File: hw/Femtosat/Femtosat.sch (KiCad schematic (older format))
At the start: 9 parts, among them J2 Programmer, U1 SAMD21G, U2 TRH-G2, U3 XA1110, Y1 32.768kHz

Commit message: Added library for certain components. Symbols and footprints were associated.
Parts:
- Cc1, Cc2: footprint Capacitor_SMD:C_0805_2012Metric_Pad1.15x1.40mm_HandSolder -> Capacitor_SMD:C_0603_1608Metric_Pad1.05x0.95mm_HandSolder
- J2: footprint (none) -> Connector_PinSocket_2.54mm:PinSocket_1x03_P2.54mm_Vertical
- U2: footprint (none) -> GPS:TRH-G2
- U3: footprint (none) -> GPS:XA1110
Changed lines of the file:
@@
 F 0 "Cc1" H 3215 2446 50  0000 L CNN
 F 1 "9pF" H 3215 2355 50  0000 L CNN
-F 2 "Capacitor_SMD:C_0805_2012Metric_Pad1.15x1.40mm_HandSolder" H 3138 2250 50  0001 C CNN
+F 2 "Capacitor_SMD:C_0603_1608Metric_Pad1.05x0.95mm_HandSolder" H 3138 2250 50  0001 C CNN
 F 3 "~" H 3100 2400 50  0001 C CNN
 	1    3100 2400
@@
 F 0 "Cc2" H 3715 2446 50  0000 L CNN
 F 1 "9pF" H 3715 2355 50  0000 L CNN
-F 2 "Capacitor_SMD:C_0805_2012Metric_Pad1.15x1.40mm_HandSolder" H 3638 2250 50  0001 C CNN
+F 2 "Capacitor_SMD:C_0603_1608Metric_Pad1.05x0.95mm_HandSolder" H 3638 2250 50  0001 C CNN
 F 3 "~" H 3600 2400 50  0001 C CNN
 	1    3600 2400
@@
 F 0 "U3" H 7600 5050 60  0000 C CNN
 F 1 "XA1110" H 7600 4350 60  0000 C CNN
-F 2 "" H 7300 4650 60  0001 C CNN
+F 2 "GPS:XA1110" H 7300 4650 60  0001 C CNN
 F 3 "" H 7300 4650 60  0001 C CNN
 	1    7600 4700
@@
 F 0 "J2" H 7572 2124 50  0000 R CNN
 F 1 "Programmer" H 7572 2033 50  0000 R CNN
-F 2 "" H 7600 2100 50  0001 C CNN
+F 2 "Connector_PinSocket_2.54mm:PinSocket_1x03_P2.54mm_Vertical" H 7600 2100 50  0001 C CNN
 F 3 "~" H 7600 2100 50  0001 C CNN
 	1    7600 2100
@@
 F 0 "U2" H 7550 3700 50  0000 C CNN
 F 1 "TRH-G2" H 7800 3050 50  0000 C CNN
-F 2 "" H 7650 3350 50  0001 C CNN
+F 2 "GPS:TRH-G2" H 7650 3350 50  0001 C CNN
 F 3 "" H 7650 3350 50  0001 C CNN
 	1    7550 3350

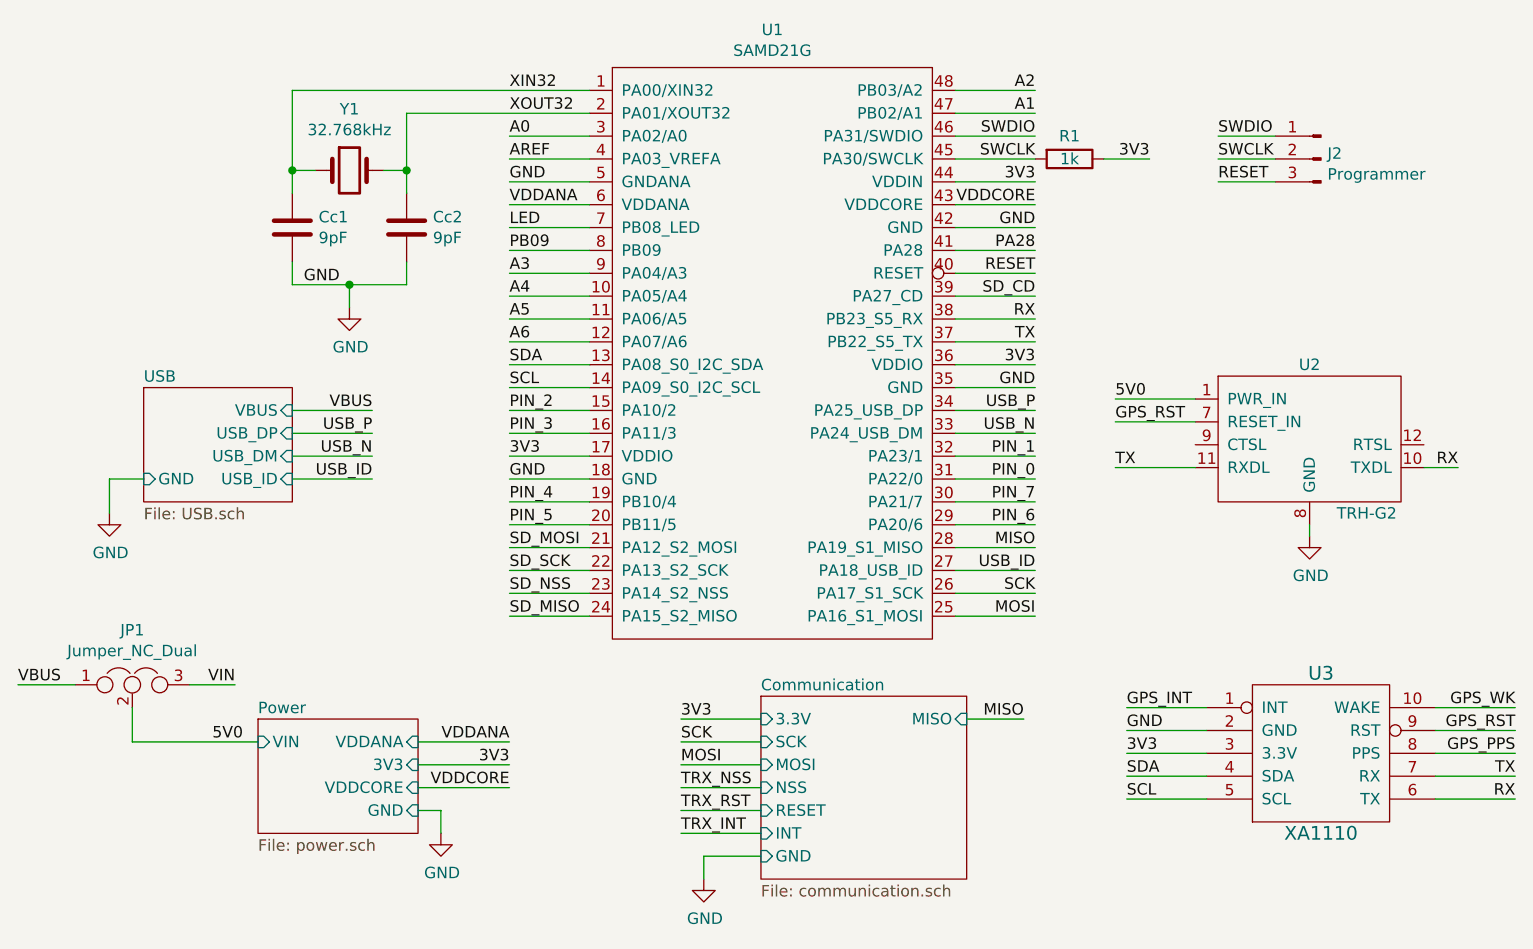
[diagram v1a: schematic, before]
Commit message: Deleted the GPS device (moved to another PCB). Added the deploy-sensor (an interrupter). Moved the programmer to its own hierarchical sheet.
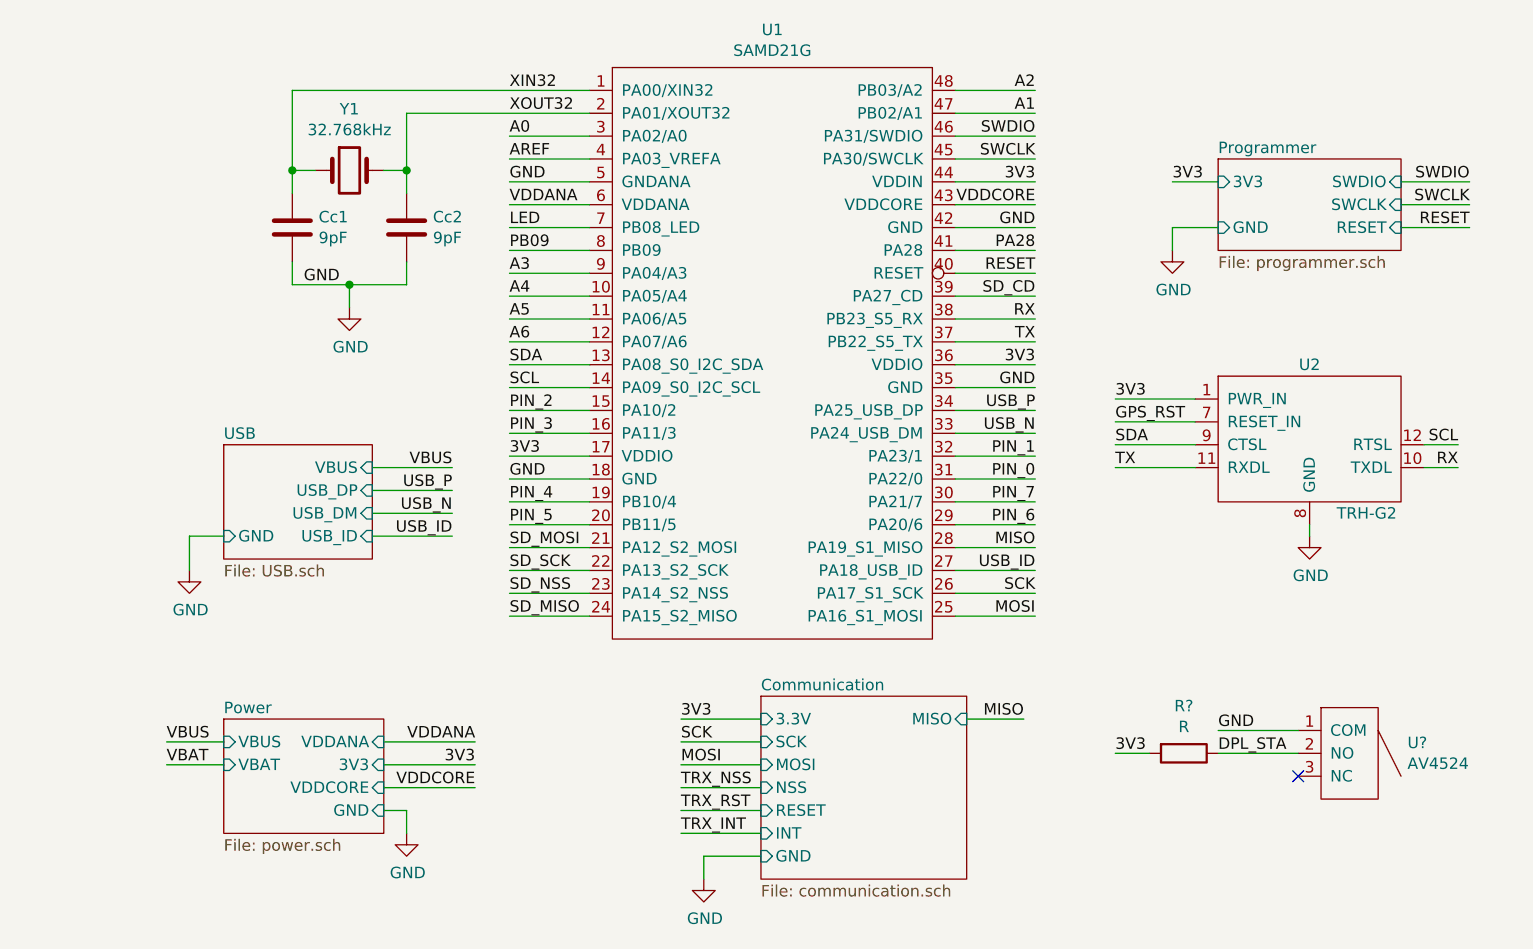
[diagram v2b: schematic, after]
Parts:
- removed J2: Programmer, Connector_PinSocket_2.54mm:PinSocket_1x03_P2.54mm_Vertical, symbol Connector:Conn_01x03_Male
- removed JP1: Jumper_NC_Dual, Connector_PinHeader_2.54mm:PinHeader_1x03_P2.54mm_Vertical, symbol Device:Jumper_NC_Dual
- removed R1: 1k, Resistor_SMD:R_0805_2012Metric_Pad1.15x1.40mm_HandSolder, symbol Device:R
- removed U3: XA1110, GPS:XA1110, symbol GPS:XA1110
- added R?: R, symbol Device:R
- added U?: AV4524, symbol Interrupter:AV4524
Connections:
- net 5V0 is gone; now on net 3V3: U2.1 (PWR_IN), U2.2 (PWR_IN)
- net 3V3: now also R?.2
- net GND: now also U?.1 (COM)
- net SCL: now also U2.12 (RTSL)
- net SDA: now also U2.9 (CTSL)
- new net DPL_STA: R?.1, U?.2 (NO)
- no-connect marks 0 -> 1
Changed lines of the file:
@@
 $Descr A4 11693 8268
 encoding utf-8
-Sheet 1 4
+Sheet 1 5
 Title ""
 Date ""
@@
 	4050 3700 4400 3700
 $Sheet
-S 2950 4550 700  500
+S 2800 4550 700  500
 U 5B6351C6
 F0 "Power" 50
 F1 "power.sch" 50
-F2 "3V3" I R 3650 4750 50
-F3 "VDDANA" I R 3650 4650 50
-F4 "VDDCORE" I R 3650 4850 50
-F5 "GND" I R 3650 4950 50
-F6 "VIN" I L 2950 4650 50
+F2 "3V3" I R 3500 4750 50
+F3 "VDDANA" I R 3500 4650 50
+F4 "VDDCORE" I R 3500 4850 50
+F5 "GND" I R 3500 4950 50
+F6 "VBUS" I L 2800 4650 50
+F7 "VBAT" I L 2800 4750 50
 $EndSheet
-Text Label 4050 4850 2    50   ~ 0
+Text Label 3900 4850 2    50   ~ 0
 VDDCORE
-Text Label 4050 4650 2    50   ~ 0
+Text Label 3900 4650 2    50   ~ 0
 VDDANA
 Wire Wire Line
-	4050 4650 3650 4650
-Wire Wire Line
-	3650 4750 4050 4750
-Wire Wire Line
-	4050 4850 3650 4850
+	3900 4650 3500 4650
+Wire Wire Line
+	3500 4750 3900 4750
+Wire Wire Line
+	3900 4850 3500 4850
 $Comp
 L Device:C Cc1
@@
 Text Label 3150 2650 0    50   ~ 0
 GND
-$Comp
-L Device:R R1
-U 1 1 5B67C5CF
-P 6500 2100
-F 0 "R1" V 6400 2100 50  0000 C CNN
-F 1 "1k" V 6500 2100 50  0000 C CNN
-F 2 "Resistor_SMD:R_0805_2012Metric_Pad1.15x1.40mm_HandSolder" V 6430 2100 50  0001 C CNN
-F 3 "~" H 6500 2100 50  0001 C CNN
-	1    6500 2100
-	0    1    1    0
-$EndComp
-Wire Wire Line
-	6650 2100 6850 2100
-Text Label 6850 2100 2    50   ~ 0
+Text Label 6950 2200 0    50   ~ 0
 3V3
 $Sheet
-S 2450 3100 650  500
+S 2800 3350 650  500
 U 5B626331
 F0 "USB" 50
 F1 "USB.sch" 50
-F2 "VBUS" I R 3100 3200 50
-F3 "USB_DP" I R 3100 3300 50
-F4 "USB_DM" I R 3100 3400 50
-F5 "USB_ID" I R 3100 3500 50
-F6 "GND" I L 2450 3500 50
+F2 "VBUS" I R 3450 3450 50
+F3 "USB_DP" I R 3450 3550 50
+F4 "USB_DM" I R 3450 3650 50
+F5 "USB_ID" I R 3450 3750 50
+F6 "GND" I L 2800 3750 50
 $EndSheet
-Text Label 3450 3300 2    50   ~ 0
+Text Label 3800 3550 2    50   ~ 0
 USB_P
 Wire Wire Line
-	3450 3300 3100 3300
-Wire Wire Line
-	3100 3200 3450 3200
-Wire Wire Line
-	3450 3400 3100 3400
-Wire Wire Line
-	3100 3500 3450 3500
-Text Label 3450 3400 2    50   ~ 0
+	3800 3550 3450 3550
+Wire Wire Line
+	3450 3450 3800 3450
+Wire Wire Line
+	3800 3650 3450 3650
+Wire Wire Line
+	3450 3750 3800 3750
+Text Label 3800 3650 2    50   ~ 0
 USB_N
-Text Label 3450 3500 2    50   ~ 0
+Text Label 3800 3750 2    50   ~ 0
 USB_ID
-Text Label 3450 3200 2    50   ~ 0
+Text Label 3800 3450 2    50   ~ 0
 VBUS
 Wire Wire Line
-	2450 3500 2300 3500
-Wire Wire Line
-	2300 3500 2300 3650
+	2800 3750 2650 3750
+Wire Wire Line
+	2650 3750 2650 3900
 $Comp
 L power:GND #PWR0104
 U 1 1 5BAA2798
-P 2300 3650
-F 0 "#PWR0104" H 2300 3400 50  0001 C CNN
-F 1 "GND" H 2305 3477 50  0000 C CNN
-F 2 "" H 2300 3650 50  0001 C CNN
-F 3 "" H 2300 3650 50  0001 C CNN
-	1    2300 3650
-	1    0    0    -1
-$EndComp
-$Comp
-L Device:Jumper_NC_Dual JP1
-U 1 1 5BADF05F
-P 2400 4400
-F 0 "JP1" H 2400 4639 50  0000 C CNN
-F 1 "Jumper_NC_Dual" H 2400 4548 50  0000 C CNN
-F 2 "Connector_PinHeader_2.54mm:PinHeader_1x03_P2.54mm_Vertical" H 2400 4400 50  0001 C CNN
-F 3 "~" H 2400 4400 50  0001 C CNN
-	1    2400 4400
-	1    0    0    -1
-$EndComp
-Wire Wire Line
-	2150 4400 1900 4400
-Text Label 1900 4400 0    50   ~ 0
+P 2650 3900
+F 0 "#PWR0104" H 2650 3650 50  0001 C CNN
+F 1 "GND" H 2655 3727 50  0000 C CNN
+F 2 "" H 2650 3900 50  0001 C CNN
+F 3 "" H 2650 3900 50  0001 C CNN
+	1    2650 3900
+	1    0    0    -1
+$EndComp
+Text Label 2550 4650 0    50   ~ 0
 VBUS
-Text Label 2850 4400 2    50   ~ 0
-VIN
-Wire Wire Line
-	2850 4400 2650 4400
-Text Label 4050 4750 2    50   ~ 0
-3V3
-Text Label 2750 4650 0    50   ~ 0
-5V0
-Wire Wire Line
-	3650 4950 3750 4950
-Wire Wire Line
-	3750 4950 3750 5050
+Text Label 3900 4750 2    50   ~ 0
+3V3
+Text Label 2550 4750 0    50   ~ 0
+VBAT
+Wire Wire Line
+	3500 4950 3600 4950
+Wire Wire Line
+	3600 4950 3600 5050
 $Comp
 L power:GND #PWR0106
 U 1 1 5BB0EE30
-P 3750 5050
-F 0 "#PWR0106" H 3750 4800 50  0001 C CNN
-F 1 "GND" H 3755 4877 50  0000 C CNN
-F 2 "" H 3750 5050 50  0001 C CNN
-F 3 "" H 3750 5050 50  0001 C CNN
-	1    3750 5050
-	1    0    0    -1
-$EndComp
-Wire Wire Line
-	2400 4650 2950 4650
-Wire Wire Line
-	2400 4500 2400 4650
-Text Label 7150 2000 0    50   ~ 0
+P 3600 5050
+F 0 "#PWR0106" H 3600 4800 50  0001 C CNN
+F 1 "GND" H 3605 4877 50  0000 C CNN
+F 2 "" H 3600 5050 50  0001 C CNN
+F 3 "" H 3600 5050 50  0001 C CNN
+	1    3600 5050
+	1    0    0    -1
+$EndComp
+Text Label 8250 2200 2    50   ~ 0
 SWDIO
-Text Label 7150 2100 0    50   ~ 0
+Text Label 8250 2300 2    50   ~ 0
 SWCLK
-Wire Wire Line
-	7400 2000 7150 2000
-Wire Wire Line
-	7150 2100 7400 2100
 $Sheet
 S 5150 4450 900  800
@@
 Wire Wire Line
 	4900 5150 4900 5250
-$Comp
-L GPS:XA1110 U3
-U 1 1 5BD2F968
-P 7600 4700
-F 0 "U3" H 7600 5050 60  0000 C CNN
-F 1 "XA1110" H 7600 4350 60  0000 C CNN
-F 2 "GPS:XA1110" H 7300 4650 60  0001 C CNN
-F 3 "" H 7300 4650 60  0001 C CNN
-	1    7600 4700
-	1    0    0    -1
-$EndComp
-Text Label 6750 4500 0    50   ~ 0
-GPS_INT
-Wire Wire Line
-	7100 4500 6750 4500
-Wire Wire Line
-	6750 4600 7100 4600
-Wire Wire Line
-	7100 4700 6750 4700
-Text Label 6750 4600 0    50   ~ 0
-GND
-Text Label 6750 4700 0    50   ~ 0
-3V3
-Text Label 6750 4800 0    50   ~ 0
-SDA
-Text Label 6750 4900 0    50   ~ 0
-SCL
-Wire Wire Line
-	7100 4800 6750 4800
-Wire Wire Line
-	6750 4900 7100 4900
-Text Label 8450 4500 2    50   ~ 0
-GPS_WK
-Text Label 8450 4600 2    50   ~ 0
-GPS_RST
-Text Label 8450 4700 2    50   ~ 0
-GPS_PPS
-Text Label 8450 4800 2    50   ~ 0
-TX
-Text Label 8450 4900 2    50   ~ 0
-RX
-Wire Wire Line
-	8450 4500 8100 4500
-Wire Wire Line
-	8100 4600 8450 4600
-Wire Wire Line
-	8450 4700 8100 4700
-Wire Wire Line
-	8100 4800 8450 4800
-Wire Wire Line
-	8450 4900 8100 4900
-$Comp
-L Connector:Conn_01x03_Male J2
-U 1 1 5BD799EE
-P 7600 2100
-F 0 "J2" H 7572 2124 50  0000 R CNN
-F 1 "Programmer" H 7572 2033 50  0000 R CNN
-F 2 "Connector_PinSocket_2.54mm:PinSocket_1x03_P2.54mm_Vertical" H 7600 2100 50  0001 C CNN
-F 3 "~" H 7600 2100 50  0001 C CNN
-	1    7600 2100
-	-1   0    0    -1
-$EndComp
-Text Label 7150 2200 0    50   ~ 0
+Text Label 8250 2400 2    50   ~ 0
 RESET
-Wire Wire Line
-	7150 2200 7400 2200
 $Comp
 L GPS:TRH-G2 U2
@@
 	8050 3450 8200 3450
 Text Label 6700 3150 0    50   ~ 0
-5V0
+3V3
 Text Label 6700 3250 0    50   ~ 0
 GPS_RST
@@
 Wire Wire Line
 	6700 3450 7050 3450
+Wire Wire Line
+	2800 4650 2550 4650
+Wire Wire Line
+	2550 4750 2800 4750
+$Comp
+L Interrupter:AV4524 U?
+U 1 1 5BFABC5E
+P 7700 4700
+F 0 "U?" H 7978 4746 50  0000 L CNN
+F 1 "AV4524" H 7978 4655 50  0000 L CNN
+F 2 "" H 7650 4700 50  0001 C CNN
+F 3 "" H 7650 4700 50  0001 C CNN
+	1    7700 4700
+	1    0    0    -1
+$EndComp
+Text Label 7150 4700 0    50   ~ 0
+DPL_STA
+Wire Wire Line
+	7150 4700 7500 4700
+Wire Wire Line
+	7150 4600 7500 4600
+Text Label 7150 4600 0    50   ~ 0
+GND
+$Comp
+L Device:R R?
+U 1 1 5BFBF6FF
+P 7000 4700
+F 0 "R?" V 6793 4700 50  0000 C CNN
+F 1 "R" V 6884 4700 50  0000 C CNN
+F 2 "" V 6930 4700 50  0001 C CNN
+F 3 "~" H 7000 4700 50  0001 C CNN
+	1    7000 4700
+	0    1    1    0
+$EndComp
+Wire Wire Line
+	6850 4700 6700 4700
+Text Label 6700 4700 0    50   ~ 0
+3V3
+NoConn ~ 7500 4800
+Wire Wire Line
+	7050 3350 6700 3350
+Wire Wire Line
+	8050 3350 8200 3350
+Text Label 6700 3350 0    50   ~ 0
+SDA
+Text Label 8200 3350 2    50   ~ 0
+SCL
+$Sheet
+S 7150 2100 800  400
+U 5BFFA937
+F0 "Programmer" 50
+F1 "programmer.sch" 50
+F2 "3V3" I L 7150 2200 50
+F3 "SWDIO" I R 7950 2200 50
+F4 "SWCLK" I R 7950 2300 50
+F5 "RESET" I R 7950 2400 50
+F6 "GND" I L 7150 2400 50
+$EndSheet
+Wire Wire Line
+	7150 2200 6950 2200
+Wire Wire Line
+	7950 2200 8250 2200
+Wire Wire Line
+	8250 2300 7950 2300
+Wire Wire Line
+	7950 2400 8250 2400
+Wire Wire Line
+	7150 2400 6950 2400
+Wire Wire Line
+	6950 2400 6950 2500
+$Comp
+L power:GND #PWR?
+U 1 1 5C018C19
+P 6950 2500
+F 0 "#PWR?" H 6950 2250 50  0001 C CNN
+F 1 "GND" H 6955 2327 50  0000 C CNN
+F 2 "" H 6950 2500 50  0001 C CNN
+F 3 "" H 6950 2500 50  0001 C CNN
+	1    6950 2500
+	1    0    0    -1
+$EndComp
 $EndSCHEMATC

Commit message: Associated the new symbols to their respective footprints.
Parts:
- R3: renamed from R?; value R -> 1k; footprint (none) -> Resistor_SMD:R_0603_1608Metric
- U3: renamed from U?; footprint (none) -> Interrupt:AV4524
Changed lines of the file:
@@
 	2550 4750 2800 4750
 $Comp
-L Interrupter:AV4524 U?
+L Interrupter:AV4524 U3
 U 1 1 5BFABC5E
 P 7700 4700
-F 0 "U?" H 7978 4746 50  0000 L CNN
+F 0 "U3" H 7978 4746 50  0000 L CNN
 F 1 "AV4524" H 7978 4655 50  0000 L CNN
-F 2 "" H 7650 4700 50  0001 C CNN
+F 2 "Interrupt:AV4524" H 7650 4700 50  0001 C CNN
 F 3 "" H 7650 4700 50  0001 C CNN
 	1    7700 4700
@@
 GND
 $Comp
-L Device:R R?
+L Device:R R3
 U 1 1 5BFBF6FF
 P 7000 4700
-F 0 "R?" V 6793 4700 50  0000 C CNN
-F 1 "R" V 6884 4700 50  0000 C CNN
-F 2 "" V 6930 4700 50  0001 C CNN
+F 0 "R3" V 6900 4700 50  0000 C CNN
+F 1 "1k" V 7000 4700 50  0000 C CNN
+F 2 "Resistor_SMD:R_0603_1608Metric" V 6930 4700 50  0001 C CNN
 F 3 "~" H 7000 4700 50  0001 C CNN
 	1    7000 4700
@@
 	6950 2400 6950 2500
 $Comp
-L power:GND #PWR?
+L power:GND #PWR0112
 U 1 1 5C018C19
 P 6950 2500
-F 0 "#PWR?" H 6950 2250 50  0001 C CNN
+F 0 "#PWR0112" H 6950 2250 50  0001 C CNN
 F 1 "GND" H 6955 2327 50  0000 C CNN
 F 2 "" H 6950 2500 50  0001 C CNN

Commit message: Routed all tracks.
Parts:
- removed R3: 1k, Resistor_SMD:R_0603_1608Metric, symbol Device:R
- removed U3: AV4524, Interrupt:AV4524, symbol Interrupter:AV4524
- added U5: XA1110, GPS:XA1110_I2C, symbol GPS:XA1110
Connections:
- net PIN_0 is gone; now on net TRX_INT: U1.31 (PA22/0)
- net PIN_6 is gone; now on net TRX_RST: U1.29 (PA20/6)
- net PIN_7 is gone; now on net TRX_NSS: U1.30 (PA21/7)
- net 3V3: now also U5.3 (3.3V)
- net GND: now also U5.2 (GND)
- net SCL: now also U5.5 (SCL); no longer U2.12 (RTSL)
- net SDA: now also U5.4 (SDA); no longer U2.9 (CTSL)
- net GPS_RST: no longer names the net of U2.7 (RESET_IN)
- no-connect marks 1 -> 9
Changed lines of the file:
@@
 Text Label 6350 3400 2    50   ~ 0
 PIN_1
-Text Label 6350 3500 2    50   ~ 0
-PIN_0
-Text Label 6350 3600 2    50   ~ 0
-PIN_7
-Text Label 6350 3700 2    50   ~ 0
-PIN_6
 Text Label 6350 3800 2    50   ~ 0
 MISO
@@
 Text Label 6700 3150 0    50   ~ 0
 3V3
-Text Label 6700 3250 0    50   ~ 0
-GPS_RST
 Text Label 6700 3450 0    50   ~ 0
 TX
@@
 	6700 3150 7050 3150
 Wire Wire Line
-	6700 3250 7050 3250
-Wire Wire Line
 	6700 3450 7050 3450
 Wire Wire Line
@@
 Wire Wire Line
 	2550 4750 2800 4750
-$Comp
-L Interrupter:AV4524 U3
-U 1 1 5BFABC5E
-P 7700 4700
-F 0 "U3" H 7978 4746 50  0000 L CNN
-F 1 "AV4524" H 7978 4655 50  0000 L CNN
-F 2 "Interrupt:AV4524" H 7650 4700 50  0001 C CNN
-F 3 "" H 7650 4700 50  0001 C CNN
-	1    7700 4700
-	1    0    0    -1
-$EndComp
-Text Label 7150 4700 0    50   ~ 0
-DPL_STA
-Wire Wire Line
-	7150 4700 7500 4700
-Wire Wire Line
-	7150 4600 7500 4600
-Text Label 7150 4600 0    50   ~ 0
-GND
-$Comp
-L Device:R R3
-U 1 1 5BFBF6FF
-P 7000 4700
-F 0 "R3" V 6900 4700 50  0000 C CNN
-F 1 "1k" V 7000 4700 50  0000 C CNN
-F 2 "Resistor_SMD:R_0603_1608Metric" V 6930 4700 50  0001 C CNN
-F 3 "~" H 7000 4700 50  0001 C CNN
-	1    7000 4700
-	0    1    1    0
-$EndComp
-Wire Wire Line
-	6850 4700 6700 4700
-Text Label 6700 4700 0    50   ~ 0
-3V3
-NoConn ~ 7500 4800
-Wire Wire Line
-	7050 3350 6700 3350
-Wire Wire Line
-	8050 3350 8200 3350
-Text Label 6700 3350 0    50   ~ 0
+Text Label 6850 4650 0    50   ~ 0
 SDA
-Text Label 8200 3350 2    50   ~ 0
+Text Label 6850 4750 0    50   ~ 0
 SCL
 $Sheet
@@
 	1    0    0    -1
 $EndComp
+$Comp
+L GPS:XA1110 U5
+U 1 1 5BFD5FD7
+P 7550 4550
+F 0 "U5" H 7550 4900 60  0000 C CNN
+F 1 "XA1110" H 7550 4200 60  0000 C CNN
+F 2 "GPS:XA1110_I2C" H 7250 4500 60  0001 C CNN
+F 3 "" H 7250 4500 60  0001 C CNN
+	1    7550 4550
+	1    0    0    -1
+$EndComp
+NoConn ~ 7050 3250
+Wire Wire Line
+	7050 4750 6850 4750
+Wire Wire Line
+	7050 4650 6850 4650
+Text Label 6850 4550 0    50   ~ 0
+3V3
+Wire Wire Line
+	7050 4550 6850 4550
+Wire Wire Line
+	7050 4450 6850 4450
+Text Label 6850 4450 0    50   ~ 0
+GND
+NoConn ~ 7050 4350
+NoConn ~ 8050 4350
+NoConn ~ 8050 4450
+NoConn ~ 8050 4550
+NoConn ~ 8050 4650
+NoConn ~ 8050 4750
+NoConn ~ 7050 3350
+NoConn ~ 8050 3350
+Text Label 6350 3500 2    50   ~ 0
+TRX_INT
+Text Label 6350 3600 2    50   ~ 0
+TRX_NSS
+Text Label 6350 3700 2    50   ~ 0
+TRX_RST
 $EndSCHEMATC
